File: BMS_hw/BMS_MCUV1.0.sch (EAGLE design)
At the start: 45 parts, among them IC2 SST25VF020B804ISA, J1 22-27-2051-05, J2 22-27-2051-05, J3 22-27-2041-04, J4 22-27-2051-05, Q2 32.768kHz, X1 87758-2016

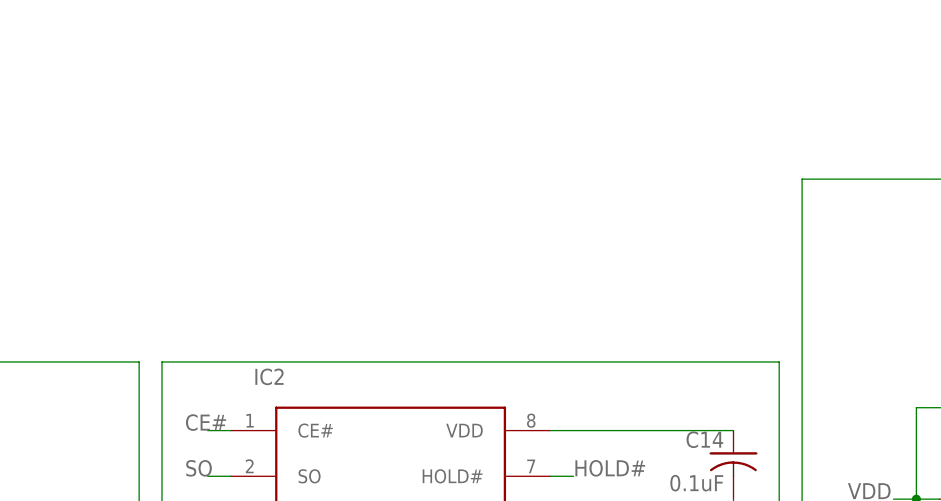
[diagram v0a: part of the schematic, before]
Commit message: mcu ldo circuit build ok
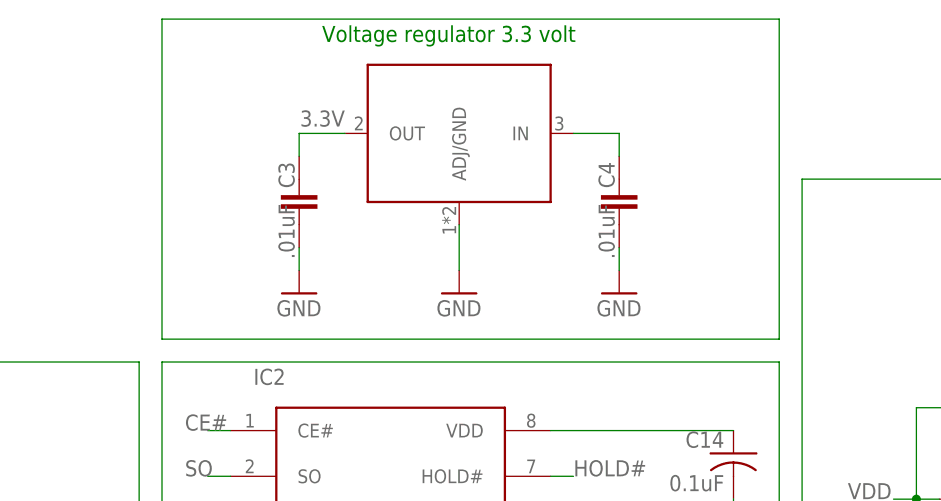
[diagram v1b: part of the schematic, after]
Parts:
- added C3, C4: .01uF, ipc-7351-capacitor:CAPACITOR_0603
- added U1: NCP1117LP-PG, GreenFuel:NCP1117LP-PG
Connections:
- new net N$5: C4.2, U1.IN
- net 3.3V: now also C3.2, U1.OUT
- net GND: now also C3.1, C4.1, U1.ADJ/GND
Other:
- note added: "Voltage regulator 3.3 volt"
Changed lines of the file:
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@@
 <setting verticaltext="up"/>
 </settings>
-<grid distance="0.1" unitdist="inch" unit="mil" style="lines" multiple="1" display="no" altdistance="0.01" altunitdist="inch" altunit="mil"/>
+<grid distance="0.1" unitdist="inch" unit="mil" style="lines" multiple="1" display="yes" altdistance="0.01" altunitdist="inch" altunit="mil"/>
 <layers>
 <layer number="1" name="Top" color="4" fill="1" visible="no" active="no"/>
@@
 <part name="C22" library="ipc-7351-capacitor" deviceset="CAPACITOR_" device="0603" value=".01uF"/>
 <part name="GND23" library="supply1" library_urn="urn:adsk.eagle:library:371" deviceset="GND" device=""/>
+<part name="U1" library="GreenFuel" deviceset="NCP1117LP" device="-PG"/>
+<part name="GND3" library="supply1" library_urn="urn:adsk.eagle:library:371" deviceset="GND" device=""/>
+<part name="C3" library="ipc-7351-capacitor" deviceset="CAPACITOR_" device="0603" value=".01uF"/>
+<part name="C4" library="ipc-7351-capacitor" deviceset="CAPACITOR_" device="0603" value=".01uF"/>
+<part name="GND4" library="supply1" library_urn="urn:adsk.eagle:library:371" deviceset="GND" device=""/>
+<part name="GND5" library="supply1" library_urn="urn:adsk.eagle:library:371" deviceset="GND" device=""/>
 </parts>
 <sheets>
@@
 600 ma ISAT
 300 ohm @ 100 MHz</text>
+<text x="233.68" y="210.82" size="1.778" layer="91">Voltage regulator 3.3 volt</text>
 </plain>
 <instances>
@@
 </instance>
 <instance part="GND23" gate="1" x="185.42" y="99.06"/>
+<instance part="U1" gate="G$1" x="248.92" y="200.66"/>
+<instance part="GND3" gate="1" x="248.92" y="182.88"/>
+<instance part="C3" gate="G$1" x="231.14" y="193.04" smashed="yes" rot="R90">
+<attribute name="NAME" x="230.632" y="194.564" size="1.778" layer="95" rot="R90"/>
+<attribute name="VALUE" x="230.632" y="186.69" size="1.778" layer="96" rot="R90"/>
+</instance>
+<instance part="C4" gate="G$1" x="266.7" y="193.04" smashed="yes" rot="R90">
+<attribute name="NAME" x="266.192" y="194.564" size="1.778" layer="95" rot="R90"/>
+<attribute name="VALUE" x="266.192" y="186.69" size="1.778" layer="96" rot="R90"/>
+</instance>
+<instance part="GND4" gate="1" x="266.7" y="182.88"/>
+<instance part="GND5" gate="1" x="231.14" y="182.88"/>
 </instances>
 <busses>
@@
 <wire x1="185.42" y1="104.14" x2="185.42" y2="101.6" width="0.1524" layer="91"/>
 </segment>
+<segment>
+<pinref part="GND5" gate="1" pin="GND"/>
+<pinref part="C3" gate="G$1" pin="1"/>
+<wire x1="231.14" y1="185.42" x2="231.14" y2="187.96" width="0.1524" layer="91"/>
+</segment>
+<segment>
+<pinref part="GND4" gate="1" pin="GND"/>
+<pinref part="C4" gate="G$1" pin="1"/>
+<wire x1="266.7" y1="185.42" x2="266.7" y2="187.96" width="0.1524" layer="91"/>
+</segment>
+<segment>
+<pinref part="GND3" gate="1" pin="GND"/>
+<pinref part="U1" gate="G$1" pin="ADJ/GND"/>
+<wire x1="248.92" y1="185.42" x2="248.92" y2="190.5" width="0.1524" layer="91"/>
+</segment>
 </net>
 <net name="N$1" class="0">
@@
 <wire x1="180.34" y1="132.08" x2="187.96" y2="132.08" width="0.1524" layer="91"/>
 <label x="187.96" y="132.08" size="1.778" layer="95" xref="yes"/>
+</segment>
+<segment>
+<pinref part="U1" gate="G$1" pin="OUT"/>
+<wire x1="236.22" y1="200.66" x2="231.14" y2="200.66" width="0.1524" layer="91"/>
+<pinref part="C3" gate="G$1" pin="2"/>
+<wire x1="231.14" y1="200.66" x2="231.14" y2="198.12" width="0.1524" layer="91"/>
+<label x="236.22" y="203.2" size="1.778" layer="95" rot="R180"/>
 </segment>
 </net>
@@
 </segment>
 </net>
+<net name="N$5" class="0">
+<segment>
+<pinref part="U1" gate="G$1" pin="IN"/>
+<wire x1="261.62" y1="200.66" x2="266.7" y2="200.66" width="0.1524" layer="91"/>
+<pinref part="C4" gate="G$1" pin="2"/>
+<wire x1="266.7" y1="200.66" x2="266.7" y2="198.12" width="0.1524" layer="91"/>
+</segment>
+</net>
+<net name="N$4" class="0">
+<segment>
+<wire x1="215.9" y1="177.8" x2="215.9" y2="213.36" width="0.1524" layer="91"/>
+<wire x1="215.9" y1="213.36" x2="284.48" y2="213.36" width="0.1524" layer="91"/>
+<wire x1="284.48" y1="213.36" x2="284.48" y2="177.8" width="0.1524" layer="91"/>
+<wire x1="284.48" y1="177.8" x2="215.9" y2="177.8" width="0.1524" layer="91"/>
+</segment>
+</net>

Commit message: erroe removed
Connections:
- net DGND renamed VSS
- removed net 12V_AUX: X1-17.S
- removed net DC_1: C13.1
- removed net GO_03: X1-5.S
- removed net GO_04: X1-15.S
- removed net HOLD#: IC2.HOLD#
- removed net ICSP_!MCLR!_VPP_TARGET: MCU2.!MCLR, R15.2
- removed net ISM: X1-1.S
- removed net KEY: X1-10.S
- removed net N$5: C4.2, U1.IN
- removed net RX_O: X1-16.S
- removed net SCL_O: X1-3.S
- removed net SDA_O: X1-13.S
- removed net SYS_VOLT: X1-8.S
- removed net SYS_VOLT_SEL: X1-18.S
- removed net TX_0: X1-6.S
- removed net T_SUPPLY: J3-1.S, J3-4.S
- removed net UC3: C7.1
- new net 15V_AUX: C4.2, U1.IN, X1-17.S
- new net DBG_RX: J3-3.S, MCU2.TDO/PMD4/RA10
- new net DBG_TX: J3-2.S, MCU2.AN9/RPA11/RA11
- new net FAULT: MCU2.OA2OUT/AN0/C2IN4-/C4IN3-/RPA0/RA0, X1-5.S
- new net N$40: MCU2.AN14/RPE14/PMA1/RE14
- new net N$41: MCU2.AN15/RPE15/PMA0/RE15
- new net N$42: MCU2.RPF0/RF0
- new net N$43: MCU2.RPF1/RF1
- new net N$44: MCU2.AN19/RPG6/PMA5/RG6
- new net N$45: MCU2.AN18/RPG7/PMA4/RG7
- new net N$46: MCU2.AN17/RPG8/PMA3/RG8
- new net N$47: MCU2.AN16/RPG9/PMA2/RG9
- new net N$66: MCU2.RPB10/PMD0/RB10
- new net N$67: MCU2.RPB11/PMD1/RB11
- new net N$68: MCU2.RPB12/PMD2/RB12
- new net N$69: MCU2.RPB13/CTPLS/PMD3/RB13
- new net N$70: MCU2.RPB15/PMD7/RB15
- new net N$71: MCU2.OA3OUT/AN6/C3IN4-/C4IN1+/C4IN4-/RPC0/RC0
- new net N$72: MCU2.OA3IN-/AN7/C3IN1-/C4IN1-/RPC1/PMA7/RC1
- new net N$73: MCU2.OA3IN+/AN8/C3IN1+/C3IN3-/RPC2/PMA13/RC2
- new net N$74: MCU2.TRCLK/RPC6/RC6
- new net N$75: MCU2.TRD0/RPC7/RC7
- new net N$76: MCU2.TRD1/RPC8/PMWR/RC8
- new net N$77: MCU2.RPC9/RC9
- new net N$78: MCU2.CDAC2/AN48/RPC10/PMA14/RC10
- new net N$79: MCU2.D1-
- new net N$80: MCU2.D1+
- new net N$81: MCU2.RPB14/VBUSON1/PMD6/RB14
- new net N$82: MCU2.VBUS, MCU2.VUSB3V3
- new net PCHG_FET: MCU2.TDI/CDAC3/AN26/RPA8/PMA9/RA8, X1-4.S
- net !MCLR: now also MCU2.!MCLR, R15.2
- net 3.3V: now also C13.1, C7.1
- net CANH: now also C9.1, R3.1, R7.2, U$1.CANH; no longer X1-14.S
- net CANL: now also C10.1, R4.1, R7.1, U$1.CANL; no longer X1-4.S
- net CAN_RX: now also MCU2.PGED3/VREF-/OA2IN-/AN2/C2IN1-/RPB0/CTED2/RB0
- net CAN_TX: now also MCU2.PGEC3/OA1OUT/VREF+/AN3/C1IN4-/C4IN2-/RPB1/CTED1/PMA6/RB1
- net CE#: now also MCU2.PGEC1/OA1IN+/AN4/C1IN1+/C1IN3-/C2IN3-/RPB2/RB2
- net C_FET: now also MCU2.OA2IN+/AN1/C2IN1+/RPA1/RA1
- net D_FET: now also MCU2.TCK/RPA7/PMD5/RA7
- net GND: now also IC2.HOLD#, J3-1.S, J3-4.S, X1-1.S, X1-10.S, X1-14.S, X1-15.S, X1-16.S, X1-18.S, X1-20.S, X1-3.S, X1-6.S, X1-8.S
- net ICSPCLK: now also MCU2.AN11/C1IN2-/PMA12/RC11
- net ICSPDAT: now also MCU2.AN10/RPA12/RA12
- net INTL_IN2: now also MCU2.OA5OUT/AN25/C5IN4-/RPB7/SCK1/INT0/RB7
- net INTL_OUT: now also MCU2.TMS/OA5IN-/AN27/C5IN1-/RPB9/RB9; no longer X1-20.S
- net ISP: now also MCU2.OA5IN+/CDAC1/AN24/C5IN1+/C5IN3-/RPA4/T1CK/RA4
- net N$10: now also MCU2.TRD3/RPD6/RD6; no longer C10.1, R4.1, R7.1, U$1.CANL
- net N$29: now also MCU2.AN12/C2IN2-/C5IN2-/PMA11/RE12; no longer J3-2.S
- net N$30: now also MCU2.AN13/C3IN2-/PMA10/RE13; no longer J3-3.S
- net N$9: now also MCU2.TRD2/RPD5/PMRD/RD5; no longer C9.1, R3.1, R7.2, U$1.CANH
- net SCK: now also MCU2.PGEC2/RPB6/SCK2/PMA15/RB6
- net SI: now also MCU2.PGED2/RPB5/USBID1/RB5
- net SO: now also MCU2.PGED1/OA1IN-/AN5/CTCMP/C1IN1-/RTCC/RPB3/RB3
- net VDD: now also X1-13.S
- net WP#: now also MCU2.RPB4/PMA8/RB4

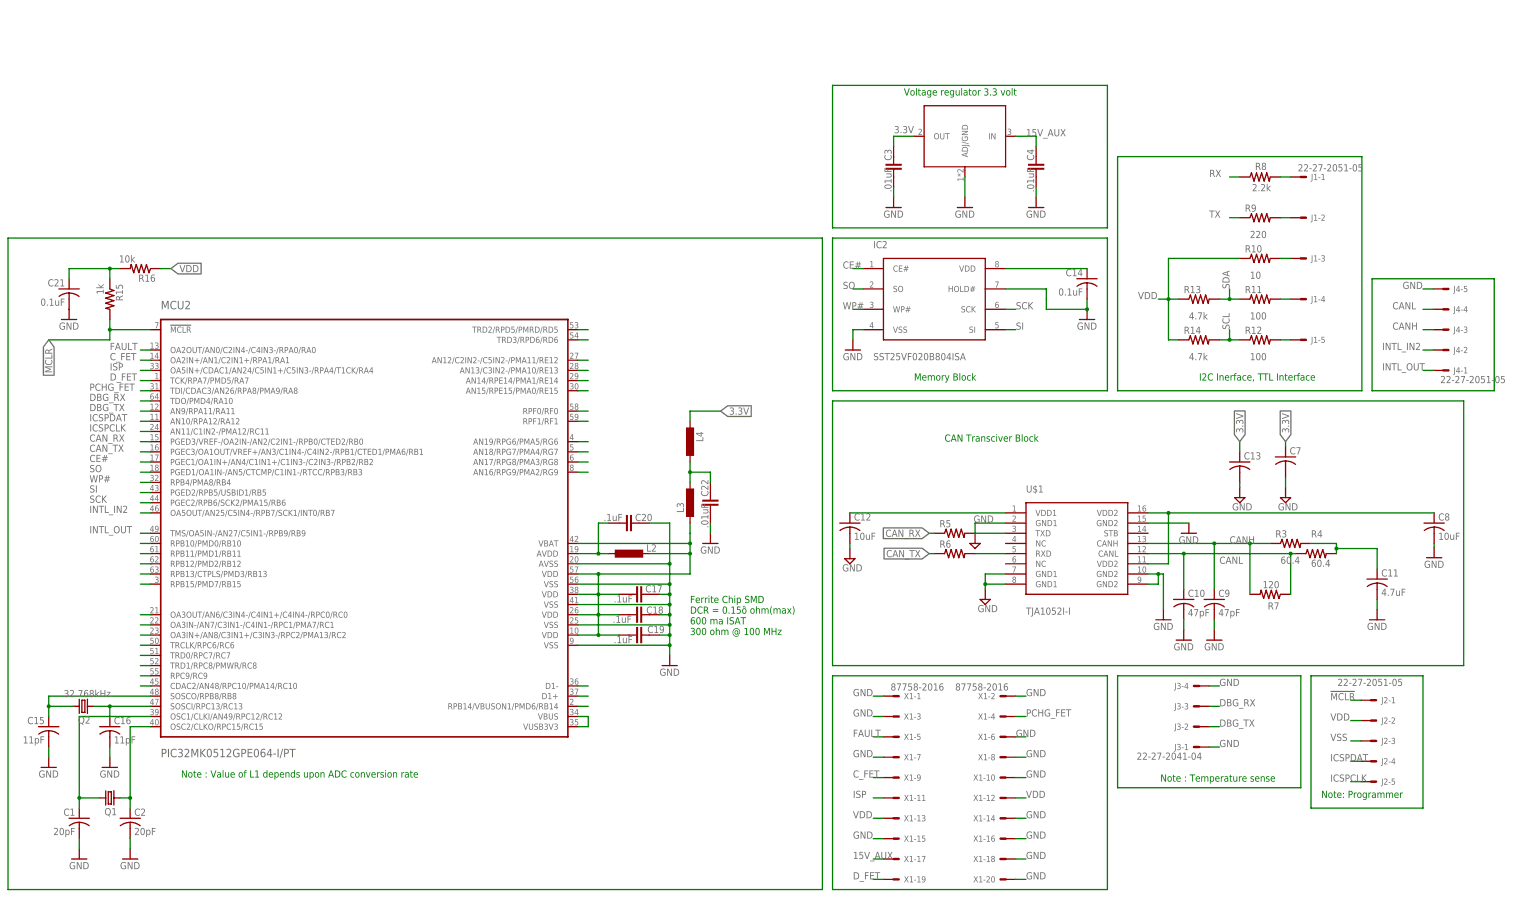
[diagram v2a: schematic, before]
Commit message: change package to 0603
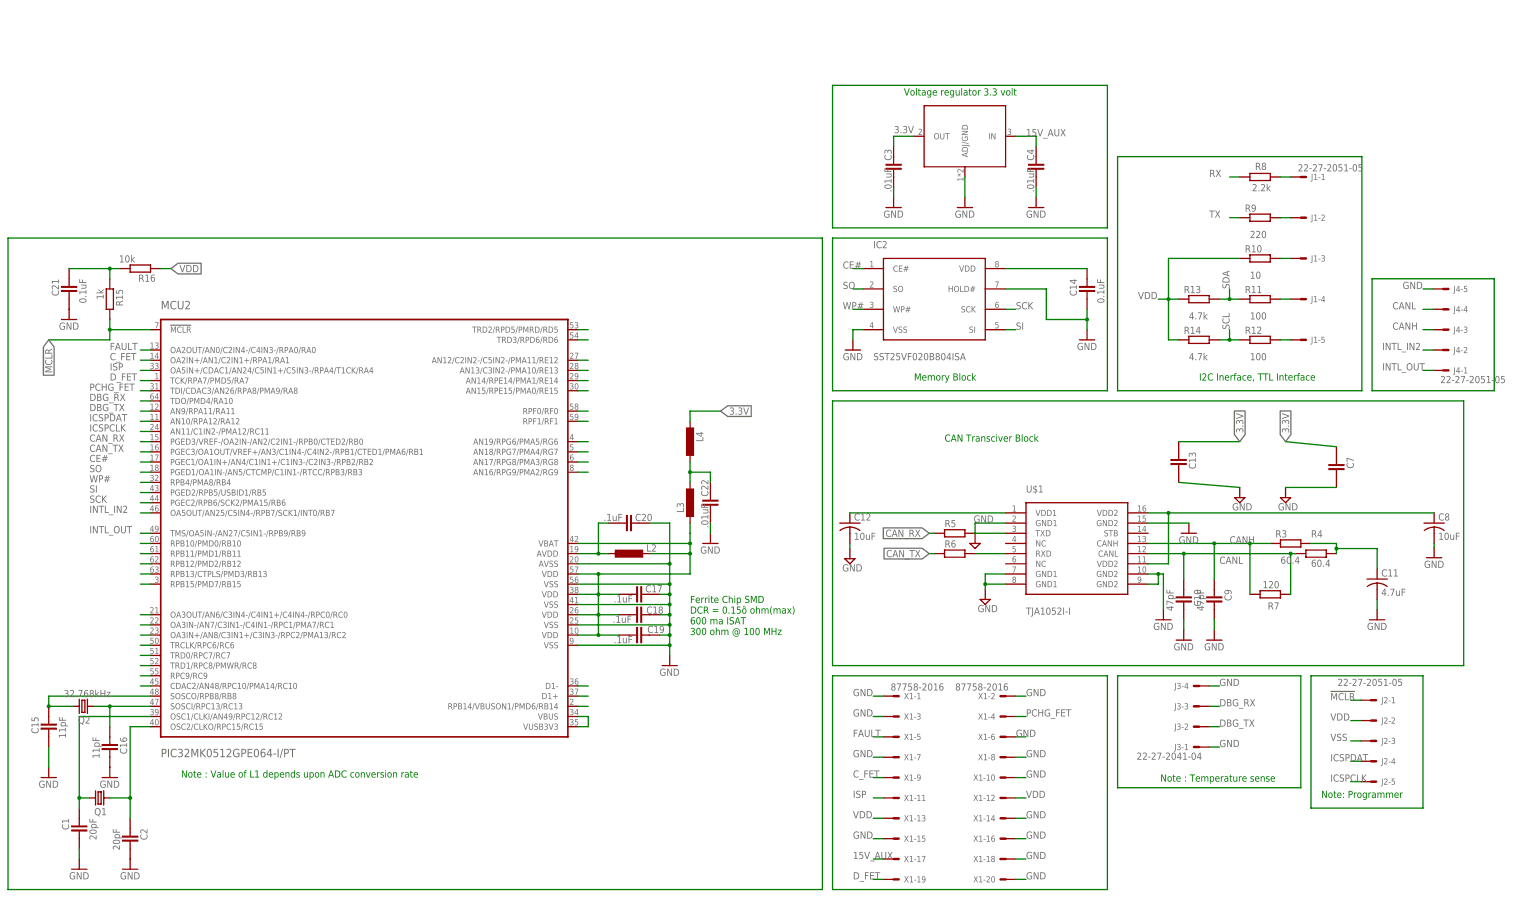
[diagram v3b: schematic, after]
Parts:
- C1, C14, C15, C16, C2, C21: device adafruit:C-USC0805 -> ipc-7351-capacitor:CAPACITOR_0603
- C10, C13, C7, C9: device adafruit:C-USC0805 -> ipc-7351-capacitor:CAPACITOR_0805
- R10, R11, R12, R13, R14, R3, R4, R5, R6, R7, R8, R9: device adafruit:R-US_M0805 -> ipc-7351-resistor:RESISTOR_0805
- R15, R16: device adafruit:R-US_R0805 -> ipc-7351-resistor:RESISTOR_0603
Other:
- moved on the sheet: C1, C10, C13, C14, C15, C16, C2, C21, C7, C9, Q1

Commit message: baord sdsahdj
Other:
- moved on the sheet: C7
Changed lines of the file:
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@@
 <setting verticaltext="up"/>
 </settings>
-<grid distance="0.1" unitdist="inch" unit="mil" style="dots" multiple="1" display="yes" altdistance="0.01" altunitdist="inch" altunit="mil"/>
+<grid distance="0.1" unitdist="inch" unit="mil" style="lines" multiple="1" display="no" altdistance="0.01" altunitdist="inch" altunit="mil"/>
 <layers>
 <layer number="1" name="Top" color="4" fill="1" visible="no" active="no"/>
@@
 <instance part="GND2" gate="1" x="40.64" y="17.78"/>
 <instance part="U$1" gate="G$1" x="276.86" y="99.06"/>
-<instance part="C7" gate="G$1" x="341.63" y="118.11" rot="R270"/>
+<instance part="C7" gate="G$1" x="340.614" y="119.38" rot="R270"/>
 <instance part="C8" gate="G$1" x="366.014" y="104.14"/>
 <instance part="C9" gate="G$1" x="311.15" y="85.09" rot="R270"/>
@@
 <instance part="C11" gate="G$1" x="351.79" y="90.17"/>
 <instance part="SUPPLY1" gate="GND" x="220.218" y="95.25"/>
-<instance part="SUPPLY2" gate="GND" x="328.93" y="110.49"/>
+<instance part="SUPPLY2" gate="GND" x="326.39" y="110.49"/>
 <instance part="SUPPLY3" gate="GND" x="317.5" y="110.49"/>
 <instance part="SUPPLY4" gate="GND" x="254" y="85.09"/>
@@
 </segment>
 <segment>
-<pinref part="C7" gate="G$1" pin="2"/>
-<pinref part="SUPPLY2" gate="GND" pin="GND"/>
-<wire x1="328.93" y1="113.03" x2="341.63" y2="113.03" width="0.1524" layer="91"/>
-</segment>
-<segment>
 <pinref part="SUPPLY1" gate="GND" pin="GND"/>
 <pinref part="C12" gate="G$1" pin="2"/>
 <wire x1="220.218" y1="97.79" x2="220.218" y2="99.06" width="0.1524" layer="91"/>
-</segment>
-<segment>
-<pinref part="SUPPLY3" gate="GND" pin="GND"/>
-<pinref part="C13" gate="G$1" pin="2"/>
-<wire x1="317.5" y1="113.03" x2="302.26" y2="114.3" width="0.1524" layer="91"/>
 </segment>
 <segment>
@@
 <junction x="175.26" y="93.98"/>
 </segment>
+<segment>
+<pinref part="C13" gate="G$1" pin="2"/>
+<wire x1="302.26" y1="114.3" x2="302.26" y2="111.76" width="0.1524" layer="91"/>
+<wire x1="302.26" y1="111.76" x2="314.96" y2="111.76" width="0.1524" layer="91"/>
+<wire x1="314.96" y1="111.76" x2="314.96" y2="114.3" width="0.1524" layer="91"/>
+<pinref part="SUPPLY3" gate="GND" pin="GND"/>
+<wire x1="314.96" y1="114.3" x2="317.5" y2="114.3" width="0.1524" layer="91"/>
+<wire x1="317.5" y1="114.3" x2="317.5" y2="113.03" width="0.1524" layer="91"/>
+</segment>
+<segment>
+<pinref part="SUPPLY2" gate="GND" pin="GND"/>
+<pinref part="C7" gate="G$1" pin="2"/>
+<wire x1="326.39" y1="113.03" x2="326.39" y2="114.3" width="0.1524" layer="91"/>
+<wire x1="326.39" y1="114.3" x2="340.614" y2="114.3" width="0.1524" layer="91"/>
+</segment>
 </net>
 <net name="N$1" class="0">
@@
 <net name="3.3V" class="0">
 <segment>
-<pinref part="L4" gate="G$1" pin="1"/>
-<wire x1="180.34" y1="129.54" x2="180.34" y2="132.08" width="0.1524" layer="91"/>
-<wire x1="180.34" y1="132.08" x2="187.96" y2="132.08" width="0.1524" layer="91"/>
-<label x="187.96" y="132.08" size="1.778" layer="95" xref="yes"/>
-</segment>
-<segment>
-<pinref part="U1" gate="G$1" pin="OUT"/>
-<wire x1="236.22" y1="200.66" x2="231.14" y2="200.66" width="0.1524" layer="91"/>
-<pinref part="C3" gate="G$1" pin="2"/>
-<wire x1="231.14" y1="200.66" x2="231.14" y2="198.12" width="0.1524" layer="91"/>
-<label x="236.22" y="203.2" size="1.778" layer="95" rot="R180"/>
-</segment>
-<segment>
 <pinref part="C13" gate="G$1" pin="1"/>
 <wire x1="302.26" y1="124.46" x2="317.5" y2="124.46" width="0.1524" layer="91"/>
@@
 <segment>
 <pinref part="C7" gate="G$1" pin="1"/>
-<wire x1="341.63" y1="123.19" x2="328.93" y2="124.46" width="0.1524" layer="91"/>
+<wire x1="340.614" y1="124.46" x2="328.93" y2="124.46" width="0.1524" layer="91"/>
 <label x="328.93" y="124.46" size="1.778" layer="95" rot="R90" xref="yes"/>
 </segment>
+<segment>
+<pinref part="U1" gate="G$1" pin="OUT"/>
+<pinref part="C3" gate="G$1" pin="2"/>
+<wire x1="236.22" y1="200.66" x2="231.14" y2="200.66" width="0.1524" layer="91"/>
+<wire x1="231.14" y1="200.66" x2="231.14" y2="198.12" width="0.1524" layer="91"/>
+<label x="231.14" y="200.66" size="1.778" layer="95"/>
+</segment>
+<segment>
+<pinref part="L4" gate="G$1" pin="1"/>
+<wire x1="180.34" y1="129.54" x2="180.34" y2="132.08" width="0.1524" layer="91"/>
+<label x="180.34" y="132.08" size="1.778" layer="95"/>
+</segment>
 </net>
